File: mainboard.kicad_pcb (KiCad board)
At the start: 4 copper layers, 44.4 x 35.8 mm, 74 parts, among them J1 Conn_01x06, J2 USB_B_Micro, J3 xf2m-2415-1a, J4 2x5 Pin Header 1.27mm, J5 Conn_01x02, J6 U.FL-R-SMT-1, J7 Conn_01x05, J8 Micro_SD_Card, SW1 KMR231NG LFS, U1 BMX160, U2 MAX706RESA+, U3 ATSAMD51J20A-M, U4 DRV8830DRC, U5 MR25H40, U6 DRV8830DRC, U7 AP2112K-3.3, U8 DRV8830DRC, U9 RFM98PW-symbols, Y1 Crystal

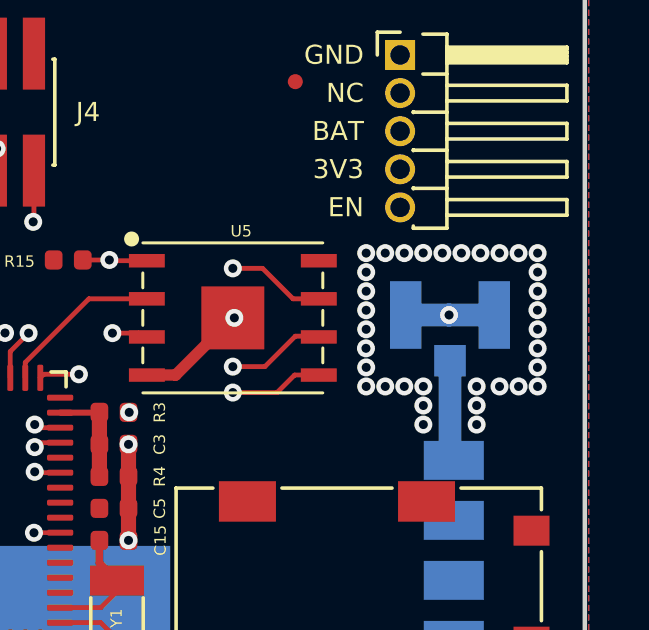
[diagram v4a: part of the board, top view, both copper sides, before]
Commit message: Expanded inner ground trace
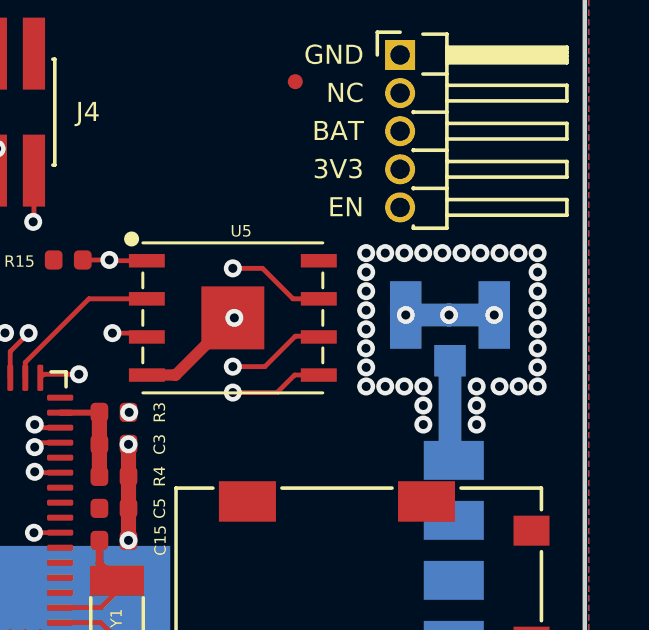
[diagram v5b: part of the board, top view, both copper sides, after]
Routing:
- net GND: vias 79 -> 81
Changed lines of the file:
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@@
   (via (at 114.8842 82.931) (size 0.6) (drill 0.3) (layers "F.Cu" "B.Cu") (free) (net 1))
   (via (at 88.4682 92.9894) (size 0.6) (drill 0.3) (layers "F.Cu" "B.Cu") (free) (net 1))
+  (via (at 117.8832 84.994) (size 0.6) (drill 0.3) (layers "F.Cu" "B.Cu") (net 1))
   (via (at 100.2538 88.0872) (size 0.6) (drill 0.3) (layers "F.Cu" "B.Cu") (net 1))
   (via (at 100.838 89.662) (size 0.6) (drill 0.3) (layers "F.Cu" "B.Cu") (net 1))
@@
   (via (at 110.998 100.7872) (size 0.6) (drill 0.3) (layers "F.Cu" "B.Cu") (net 1))
   (via (at 119.1514 95.885) (size 0.6) (drill 0.3) (layers "F.Cu" "B.Cu") (net 1))
+  (via (at 114.9332 84.994) (size 0.6) (drill 0.3) (layers "F.Cu" "B.Cu") (net 1))
   (via (at 119.3292 82.931) (size 0.6) (drill 0.3) (layers "F.Cu" "B.Cu") (free) (net 1))
   (via (at 79.0956 83.5152) (size 0.6) (drill 0.3) (layers "F.Cu" "B.Cu") (net 1))
@@
   (segment (start 90.6526 98.3996) (end 90.6374 98.4148) (width 0.508) (layer "F.Cu") (net 61))
   (via (at 90.6526 98.3996) (size 0.6) (drill 0.3) (layers "F.Cu" "B.Cu") (net 61))
-  (segment (start 107.8484 98.679) (end 107.8484 83.0326) (width 0.762) (layer "In2.Cu") (net 61))
-  (segment (start 104.7369 101.7905) (end 107.8484 98.679) (width 0.762) (layer "In2.Cu") (net 61))
-  (segment (start 107.8484 83.0326) (end 109.474 81.407) (width 0.762) (layer "In2.Cu") (net 61))
+  (segment (start 109.347 81.407) (end 114.745211 81.407) (width 0.762) (layer "In2.Cu") (net 61))
+  (segment (start 107.442 83.312) (end 109.347 81.407) (width 0.762) (layer "In2.Cu") (net 61))
+  (segment (start 104.3305 101.7905) (end 107.442 98.679) (width 0.762) (layer "In2.Cu") (net 61))
+  (segment (start 90.6526 98.3996) (end 90.7034 98.3996) (width 0.762) (layer "In2.Cu") (net 61))
   (segment (start 90.7034 98.3996) (end 94.0943 101.7905) (width 0.762) (layer "In2.Cu") (net 61))
-  (segment (start 90.6526 98.3996) (end 90.7034 98.3996) (width 0.762) (layer "In2.Cu") (net 61))
-  (segment (start 109.474 81.407) (end 114.745211 81.407) (width 0.762) (layer "In2.Cu") (net 61))
-  (segment (start 94.0943 101.7905) (end 104.7369 101.7905) (width 0.762) (layer "In2.Cu") (net 61))
+  (segment (start 107.442 98.679) (end 107.442 83.312) (width 0.762) (layer "In2.Cu") (net 61))
+  (segment (start 94.0943 101.7905) (end 104.3305 101.7905) (width 0.762) (layer "In2.Cu") (net 61))
   (segment (start 85.979 99.8982) (end 86.3956 100.3148) (width 0.16) (layer "F.Cu") (net 68))
   (segment (start 85.979 99.3926) (end 85.979 99.8982) (width 0.16) (layer "F.Cu") (net 68))
@@
     (polygon
       (pts
-        (xy 121.2342 92.8624)
-        (xy 107.2642 92.8624)
-        (xy 107.2642 72.4154)
+        (xy 121.2342 109.2454)
+        (xy 105.4862 109.2454)
+        (xy 105.4862 72.4154)
         (xy 121.2342 72.4154)
       )

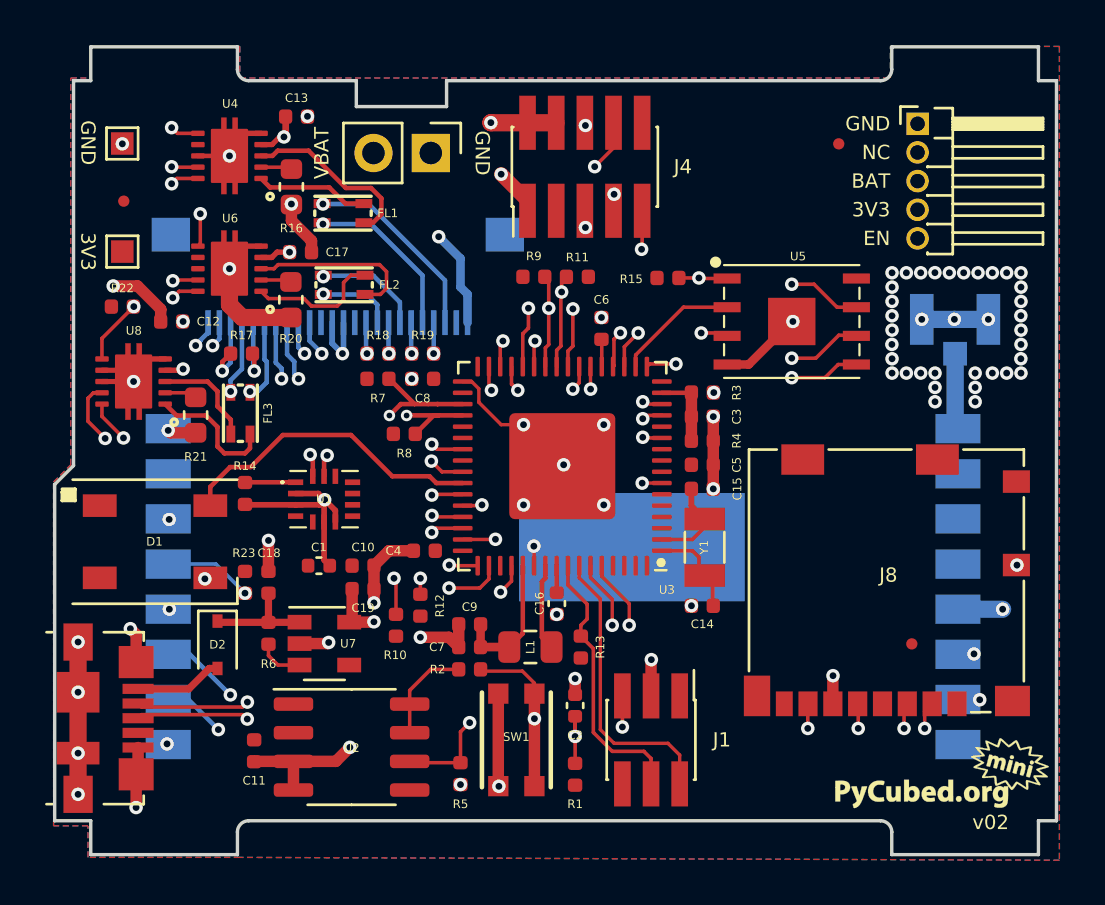
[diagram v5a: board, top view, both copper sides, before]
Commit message: Moved RBF Header to under micro USB port
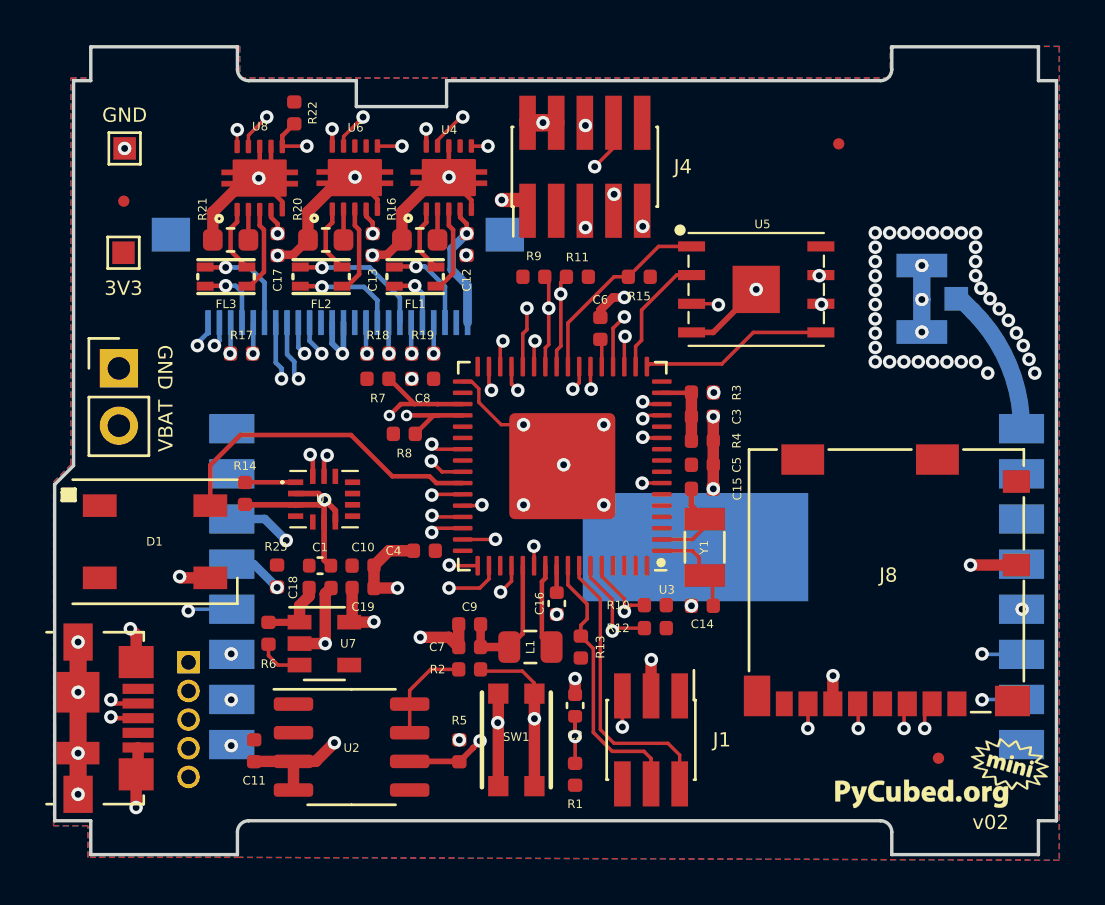
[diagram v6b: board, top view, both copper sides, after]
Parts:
- removed D2: RB550V, Diode_SMD:D_SOD-323
- J7: moved to B.Cu
- moved J7 40.2 mm to (82.4, 100.2), turned to 180 degrees
- moved J5 16.8 mm to (79.3, 87.2), turned to 0 degrees
- moved C12 13.5 mm to (94.8, 81.7), turned to -90 degrees
- moved R10 11.5 mm to (103.1, 97.7), turned to 0 degrees
- moved R22 11.5 mm to (87.1, 75.8), turned to -90 degrees
- moved U8 10.6 mm to (85.6, 78.7), turned to 90 degrees
- moved R12 10.5 mm to (103.1, 98.7), turned to 0 degrees
- moved U4 9.77 mm to (94.0, 78.7), turned to 90 degrees
- moved R21 7.91 mm to (84.3, 81.5), turned to 0 degrees
- moved U6 6.87 mm to (89.8, 78.7), turned to 90 degrees
- moved C13 6.60 mm to (90.6, 81.7), turned to -90 degrees
- moved R16 6.15 mm to (92.7, 81.5), turned to 0 degrees
- moved FL3 6.09 mm to (84.1, 83.1), turned to 180 degrees
- moved FID1 5.20 mm to (115.7, 104.4)
- moved FL1 4.26 mm to (92.5, 83.1)
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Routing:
- net Net-(C19-Pad1): track 45.6 -> 16.9 mm
- net BATT_P: track 95.0 -> 118.0 mm, vias 8 -> 6
- net M_FAULT: track 36.1 -> 24.6 mm
- net GND: track 87.0 -> 96.0 mm
- net SDA3: track 52.2 -> 45.8 mm, vias 5 -> 4
- net MOSI: track 70.0 -> 64.7 mm
- net USB_D-: track 18.7 -> 23.5 mm
- net COIL2_N: track 7.45 -> 2.69 mm
- net COIL1_P: track 8.68 -> 4.23 mm
- net MISO: track 68.4 -> 64.2 mm
- net Net-(FL1-Pad1): track 7.94 -> 3.91 mm
- net USB_D+: track 19.7 -> 23.6 mm
- net VUSB: track 3.89 -> 0.00 mm
- net Net-(FL2-Pad1): track 7.57 -> 3.94 mm
- net RF_CS: track 15.9 -> 12.4 mm
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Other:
- rule pad_to_mask_clearance: 0.049 -> 0.0508

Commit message: Updated 3D Models
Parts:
- removed the Ref** at (111.9, 79.5)
- added D2: RB550V, Diode_SMD:D_SOD-323, F.Cu at (84.3, 99.6)
- FL1, FL2, FL3: footprint wbraun_smd:SRF2012 -> pycubed:SRF2012
- J6: footprint UFL-R:U.FL-R-SMT-1 -> pycubed:U.FL-R-SMT-1
- J8: footprint Connector_Card:microSD_HC_Molex_104031-0811 -> pycubed:microSD_HC_Molex_104031-0811
- SW1: footprint Adafruit Feather M4 Express:BTN_KMR2_4.6X2.8 -> pycubed:BTN_KMR2_4.6X2.8
- U1: footprint custom-footprints:BMX160 -> pycubed:BMX160
- U2: footprint Package_SO:SO-8_3.9x4.9mm_P1.27mm -> Package_SO:SOIC-8_3.9x4.9mm_P1.27mm
- U4, U6, U8: footprint wbraun_smd:VSON-10 -> pycubed:VSON-10
- U5: footprint MR25H40:SON127P600X500X90-9N -> pycubed:SON127P600X500X90-9N
- Y1: footprint Crystal:Crystal_SMD_3215-2Pin_3.2x1.5mm -> Crystal:Crystal_SMD_MicroCrystal_CC7V-T1A-2Pin_3.2x1.5mm
- moved FID1 7.10 mm to (108.6, 104.0)
- moved J8 2.79 mm to (113.4, 93.8)
- moved Ref** 2.14 mm to (114.8, 103.2)
- moved R12 2.06 mm to (101.3, 97.7), turned to -90 degrees
- moved R10 0.82 mm to (102.3, 97.7), turned to -90 degrees
- moved J2 0.18 mm to (78.9, 102.7)
- moved C16 0.15 mm to (98.8, 97.7)
- moved J7 0.14 mm to (82.3, 100.2)
- moved R6 0.13 mm to (85.9, 98.9)
- moved C6 0.10 mm to (100.7, 85.3)
- moved C4 0.08 mm to (92.8, 95.2)
- moved R20 0.07 mm to (88.4, 81.5)
- moved R21 0.07 mm to (84.2, 81.5)
- moved L1 0.05 mm to (97.6, 99.6)
- turned Y1 to 90 degrees
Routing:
- net VUSB: track 0.00 -> 7.29 mm
- net SCL3: track 45.5 -> 39.5 mm
- net SDA3: track 45.8 -> 42.2 mm
- net MOSI: track 64.7 -> 68.1 mm
- net MISO: track 64.2 -> 66.7 mm
- net Net-(C18-Pad1): track 3.07 -> 4.77 mm
- net BATT_P: track 118.0 -> 116.6 mm
- net SD_CS: track 20.2 -> 18.8 mm
- net ~{RESET}: track 23.5 -> 22.6 mm
- net GND: track 96.0 -> 95.4 mm
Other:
- board text added: "ANT"
- board text added: "BATT_P"
- board text added: "MISO"
- board text added: "MOSI"
- board text added: "RF_CS"
- board text added: "RF_IO0"
- board text added: "RF_IO1"
- board text added: "RF_RST"
- board text added: "SCK"
- board text removed: "Ant"
